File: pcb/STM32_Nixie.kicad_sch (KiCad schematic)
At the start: 0 parts

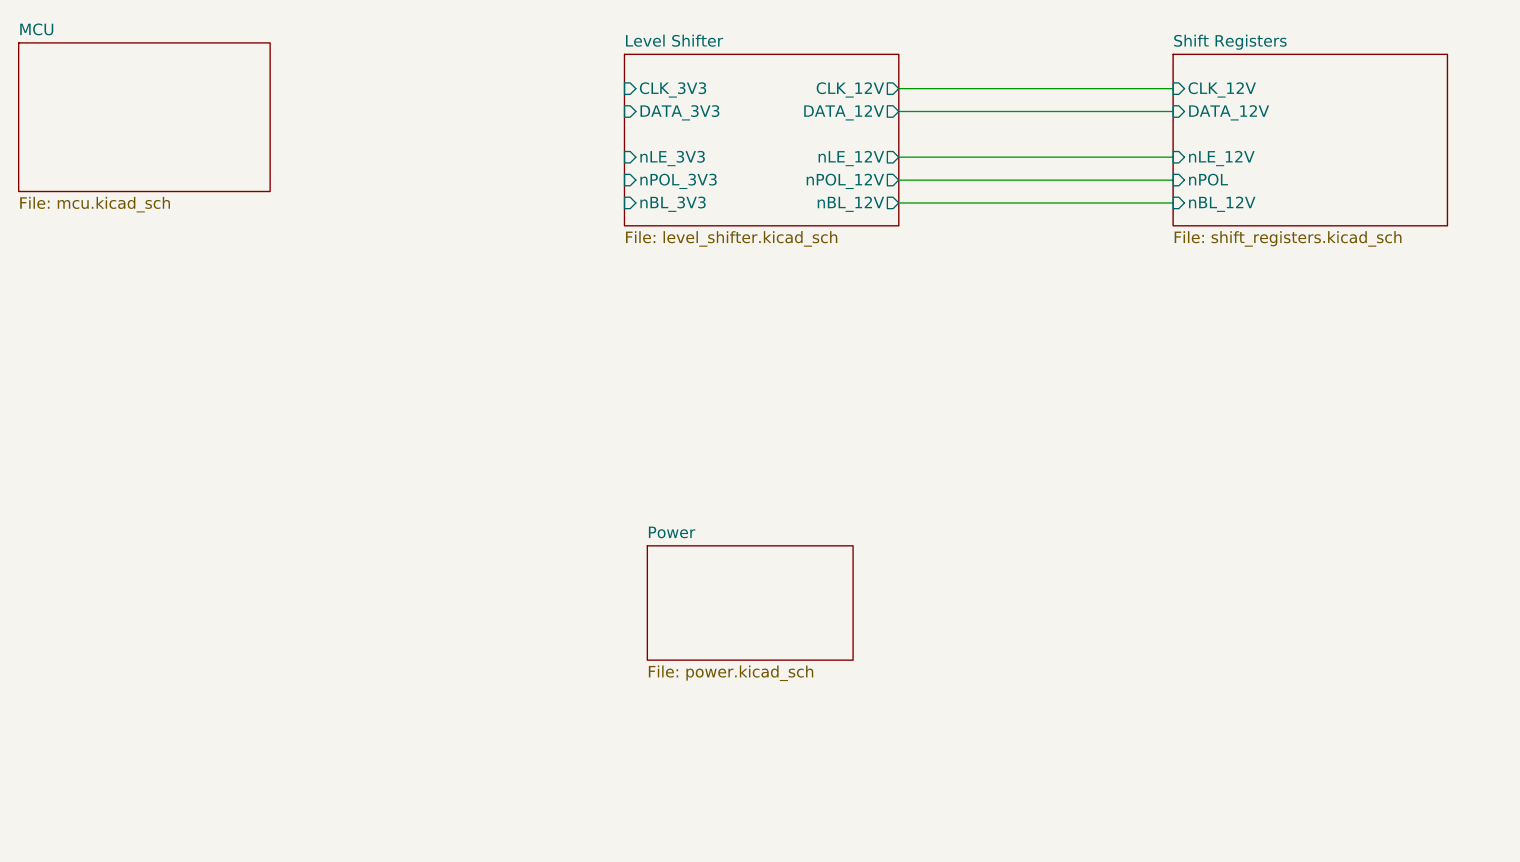
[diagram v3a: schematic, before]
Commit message: Added 8MHz Oscillator and mapped most of the MCU pins"
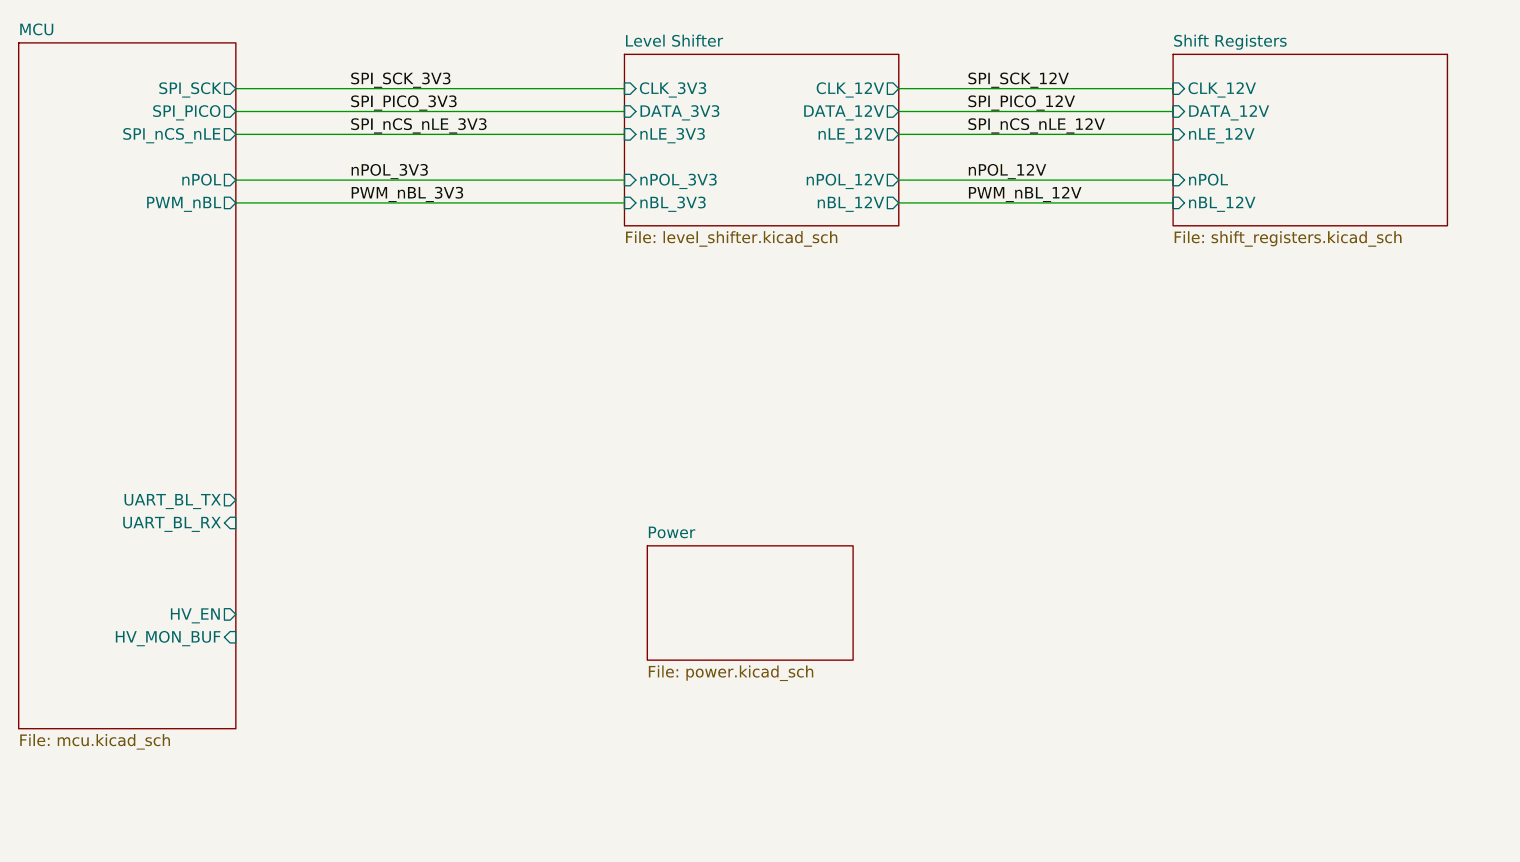
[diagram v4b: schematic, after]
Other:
- sheet MCU ports: added HV_EN, HV_MON_BUF, PWM_nBL, SPI_PICO, SPI_SCK, SPI_nCS_nLE, UART_BL_RX, UART_BL_TX, nPOL; removed none

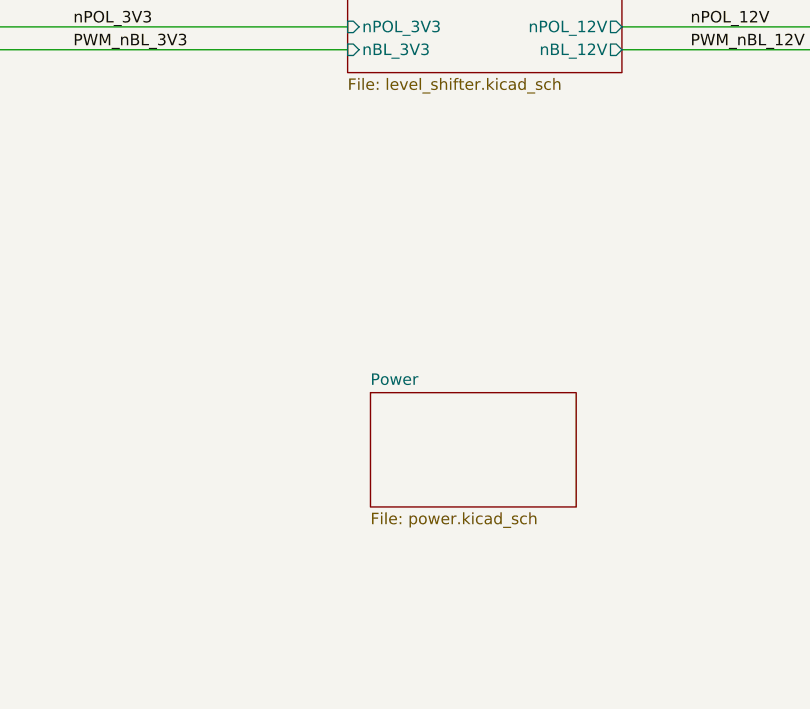
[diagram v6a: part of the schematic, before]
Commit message: Changed Boot0 switch to mom. pb, added rotary encoder, and nRST pb
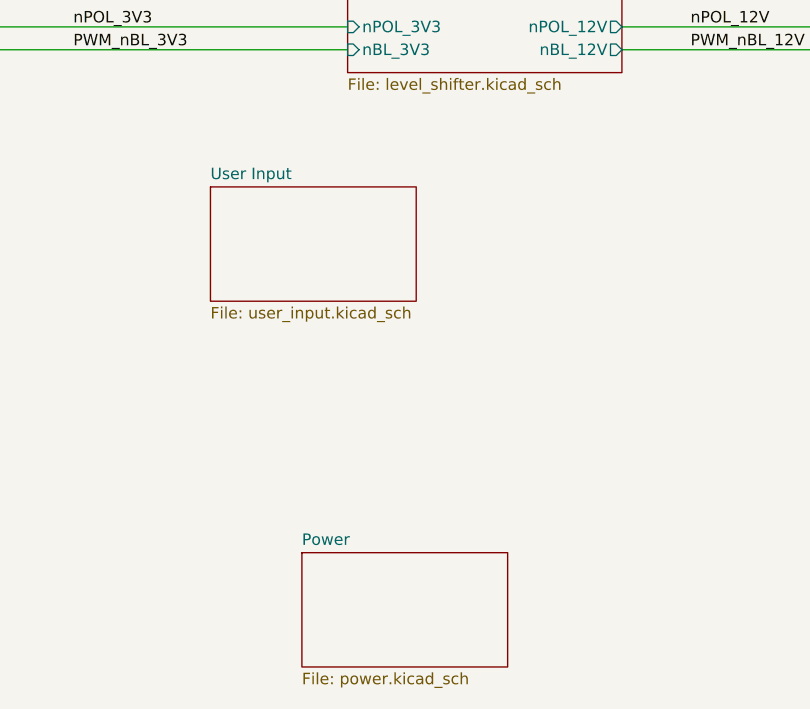
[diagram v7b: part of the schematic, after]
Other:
- added sheet User Input (user_input.kicad_sch)
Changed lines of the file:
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@@
+    )
+  )
+  (sheet (at 119.38 99.06) (size 22.86 12.7) (fields_autoplaced)
+    (stroke (width 0.1524) (type solid) (color 0 0 0 0))
+    (fill (color 0 0 0 0.0000))
+    (property "Sheet name" "User Input" (id 0) (at 119.38 98.3484 0)
+      (effects (font (size 1.27 1.27)) (justify left bottom))
+    )
+    (property "Sheet file" "user_input.kicad_sch" (id 1) (at 119.38 112.3446 0)
+      (effects (font (size 1.27 1.27)) (justify left top))
     )
   )
@@
     )
   )
-  (sheet (at 137.16 121.92) (size 22.86 12.7) (fields_autoplaced)
+  (sheet (at 129.54 139.7) (size 22.86 12.7) (fields_autoplaced)
     (stroke (width 0.1524) (type solid) (color 0 0 0 0))
     (fill (color 0 0 0 0.0000))
-    (property "Sheet name" "Power" (id 0) (at 137.16 121.2084 0)
+    (property "Sheet name" "Power" (id 0) (at 129.54 138.9884 0)
       (effects (font (size 1.27 1.27)) (justify left bottom))
     )
-    (property "Sheet file" "power.kicad_sch" (id 1) (at 137.16 135.2046 0)
+    (property "Sheet file" "power.kicad_sch" (id 1) (at 129.54 152.9846 0)
       (effects (font (size 1.27 1.27)) (justify left top))
     )
@@
     (path "/307c8046-6a25-4c40-9f6b-0df19175f959" (page "10"))
     (path "/b6f49995-0eb9-4525-a397-4f1a1965a188" (page "11"))
+    (path "/7f1e094c-d2d9-45ca-af31-f2b20e969c41" (page "12"))
   )
   (symbol_instances
@@
       (reference "#PWR039") (unit 1) (value "GND") (footprint "")
     )
-    (path "/8ecdbb98-5b2a-4725-a227-62b58d0c66f3/80efdaf2-d5a3-4a81-adba-53a920337fb2"
-      (reference "#PWR?") (unit 1) (value "GND") (footprint "")
+    (path "/8ecdbb98-5b2a-4725-a227-62b58d0c66f3/cf3a7745-9e48-408c-810d-2662e07bc0fd"
+      (reference "#PWR040") (unit 1) (value "GND") (footprint "")
+    )
+    (path "/8ecdbb98-5b2a-4725-a227-62b58d0c66f3/c260bd7e-1970-44f1-8460-f04872940c93"
+      (reference "#PWR041") (unit 1) (value "+3.3V") (footprint "")
+    )
+    (path "/8ecdbb98-5b2a-4725-a227-62b58d0c66f3/e98dab80-82d5-44b0-b230-3d2a8dc0b464"
+      (reference "#PWR042") (unit 1) (value "+3.3V") (footprint "")
     )
     (path "/8ecdbb98-5b2a-4725-a227-62b58d0c66f3/94413c1a-988b-4fe0-9e4f-82a46b39c491"
-      (reference "#PWR?") (unit 1) (value "+3.3V") (footprint "")
-    )
-    (path "/8ecdbb98-5b2a-4725-a227-62b58d0c66f3/c260bd7e-1970-44f1-8460-f04872940c93"
-      (reference "#PWR?") (unit 1) (value "+3.3V") (footprint "")
-    )
-    (path "/8ecdbb98-5b2a-4725-a227-62b58d0c66f3/cf3a7745-9e48-408c-810d-2662e07bc0fd"
-      (reference "#PWR?") (unit 1) (value "GND") (footprint "")
+      (reference "#PWR044") (unit 1) (value "+3.3V") (footprint "")
     )
     (path "/8ecdbb98-5b2a-4725-a227-62b58d0c66f3/e278a8ec-5721-40bf-b2cb-6783be8e79cc"
-      (reference "#PWR?") (unit 1) (value "GND") (footprint "")
-    )
-    (path "/8ecdbb98-5b2a-4725-a227-62b58d0c66f3/e98dab80-82d5-44b0-b230-3d2a8dc0b464"
-      (reference "#PWR?") (unit 1) (value "+3.3V") (footprint "")
+      (reference "#PWR045") (unit 1) (value "GND") (footprint "")
+    )
+    (path "/7f1e094c-d2d9-45ca-af31-f2b20e969c41/e2b85829-8087-4caf-9ed9-28a9ad4f2e8b"
+      (reference "#PWR046") (unit 1) (value "+3.3V") (footprint "")
+    )
+    (path "/7f1e094c-d2d9-45ca-af31-f2b20e969c41/5959c917-a90c-46b2-b99d-437e6ede76e2"
+      (reference "#PWR047") (unit 1) (value "+3.3V") (footprint "")
+    )
+    (path "/7f1e094c-d2d9-45ca-af31-f2b20e969c41/f952946d-ec4b-49ef-8ff1-1d14625955d8"
+      (reference "#PWR048") (unit 1) (value "+3.3V") (footprint "")
+    )
+    (path "/7f1e094c-d2d9-45ca-af31-f2b20e969c41/19018160-5b5b-47ae-84ef-f67b309cee66"
+      (reference "#PWR?") (unit 1) (value "GND") (footprint "")
+    )
+    (path "/7f1e094c-d2d9-45ca-af31-f2b20e969c41/351dfe6b-16a0-4dba-9ac7-f48d92dbd7ed"
+      (reference "#PWR?") (unit 1) (value "GND") (footprint "")
+    )
+    (path "/7f1e094c-d2d9-45ca-af31-f2b20e969c41/47d8c42e-645b-4356-a938-8a84eae8836c"
+      (reference "#PWR?") (unit 1) (value "GND") (footprint "")
+    )
+    (path "/8ecdbb98-5b2a-4725-a227-62b58d0c66f3/47f66aef-bce2-4ea4-8203-d99f7ba5bc8a"
+      (reference "#PWR?") (unit 1) (value "GND") (footprint "")
+    )
+    (path "/7f1e094c-d2d9-45ca-af31-f2b20e969c41/93f56527-ed39-45e7-a1af-7c9fbc290d95"
+      (reference "#PWR?") (unit 1) (value "GND") (footprint "")
+    )
+    (path "/8ecdbb98-5b2a-4725-a227-62b58d0c66f3/97741534-c870-41b3-b484-64d38a10e59f"
+      (reference "#PWR?") (unit 1) (value "GND") (footprint "")
     )
     (path "/8ecdbb98-5b2a-4725-a227-62b58d0c66f3/82d4e7bc-49e8-418b-8c34-f46f3717b905"
@@
       (reference "C19") (unit 1) (value "CAP_CER_4700p_250V_X7R_0805") (footprint "Capacitor_SMD:C_0805_2012Metric")
     )
+    (path "/7f1e094c-d2d9-45ca-af31-f2b20e969c41/4efb7186-35ee-4dab-b3aa-45ce8c158935"
+      (reference "C20") (unit 1) (value "CAP_CER_0u01_50V_X7R_0603") (footprint "Capacitor_SMD:C_0603_1608Metric")
+    )
+    (path "/7f1e094c-d2d9-45ca-af31-f2b20e969c41/8596294f-c74b-4e50-b6cc-c3dc23669cc2"
+      (reference "C21") (unit 1) (value "CAP_CER_0u01_50V_X7R_0603") (footprint "Capacitor_SMD:C_0603_1608Metric")
+    )
+    (path "/7f1e094c-d2d9-45ca-af31-f2b20e969c41/4552bd68-7e86-463c-ba01-3ba48b18d938"
+      (reference "C22") (unit 1) (value "CAP_CER_0u01_50V_X7R_0603") (footprint "Capacitor_SMD:C_0603_1608Metric")
+    )
     (path "/8ecdbb98-5b2a-4725-a227-62b58d0c66f3/f1a32571-49a9-4e57-8b0e-76d78478425a"
       (reference "FB1") (unit 1) (value "FER_1K_600mA_0603") (footprint "Inductor_SMD:L_0603_1608Metric")
@@
     )
     (path "/8ecdbb98-5b2a-4725-a227-62b58d0c66f3/bea2fbe2-f567-481e-90f0-85d9663358e6"
-      (reference "J?") (unit 1) (value "CON_SAMTEC_14P_2R_1m27_P_KEY_FTSH-107-01-L-DV-K-TR") (footprint "arjun_footprints:CON_FTSH-107-01-x-DV-K")
+      (reference "J2") (unit 1) (value "CON_SAMTEC_14P_2R_1m27_P_KEY_FTSH-107-01-L-DV-K-TR") (footprint "arjun_footprints:CON_FTSH-107-01-x-DV-K")
     )
     (path "/8ecdbb98-5b2a-4725-a227-62b58d0c66f3/271153ea-9406-4185-bebd-7bb424efc536"
-      (reference "JP?") (unit 1) (value "SolderJumper_3_Bridged12") (footprint "Jumper:SolderJumper-3_P1.3mm_Bridged12_RoundedPad1.0x1.5mm_NumberLabels")
+      (reference "JP1") (unit 1) (value "SolderJumper_3_Bridged12") (footprint "Jumper:SolderJumper-3_P1.3mm_Bridged12_RoundedPad1.0x1.5mm_NumberLabels")
     )
     (path "/f14ed119-44a4-4dba-a5a7-78813bb44ce1/47fb6452-bb5d-491d-bdc1-b44524035875/592da241-0f55-4f7a-a38f-5ee5a4570347"
@@
     )
     (path "/8ecdbb98-5b2a-4725-a227-62b58d0c66f3/4bdcf741-9b10-451e-b4b3-0d8c758e628e"
-      (reference "R?") (unit 1) (value "RES_10K_1P_1/10W_0603") (footprint "Resistor_SMD:R_0603_1608Metric")
+      (reference "R15") (unit 1) (value "RES_10K_1P_1/10W_0603") (footprint "Resistor_SMD:R_0603_1608Metric")
     )
     (path "/8ecdbb98-5b2a-4725-a227-62b58d0c66f3/4d1cfcde-8dbf-411d-acac-ae2b684de1a4"
-      (reference "R?") (unit 1) (value "RES_10K_1P_1/10W_0603") (footprint "Resistor_SMD:R_0603_1608Metric")
-    )
-    (path "/8ecdbb98-5b2a-4725-a227-62b58d0c66f3/8b537fd6-9959-4c0c-af54-290b92d638d2"
-      (reference "SW?") (unit 1) (value "SW_SPDT_12V_100mA_OS102011MS2QN1") (footprint "arjun_footprints:SW_OS102011MS2QN1")
+      (reference "R16") (unit 1) (value "RES_10K_1P_1/10W_0603") (footprint "Resistor_SMD:R_0603_1608Metric")
+    )
+    (path "/7f1e094c-d2d9-45ca-af31-f2b20e969c41/8aa479a8-4aeb-4d59-a85f-fc41d653df67"
+      (reference "R17") (unit 1) (value "RES_10K_1P_1/10W_0603") (footprint "Resistor_SMD:R_0603_1608Metric")
+    )
+    (path "/7f1e094c-d2d9-45ca-af31-f2b20e969c41/47e1e6e2-cd19-4e54-ab53-5d73e6984888"
+      (reference "R18") (unit 1) (value "RES_10K_1P_1/10W_0603") (footprint "Resistor_SMD:R_0603_1608Metric")
+    )
+    (path "/7f1e094c-d2d9-45ca-af31-f2b20e969c41/5d6e53eb-9333-4cc5-a8b9-529f63aa4c5e"
+      (reference "R19") (unit 1) (value "RES_10K_1P_1/10W_0603") (footprint "Resistor_SMD:R_0603_1608Metric")
+    )
+    (path "/7f1e094c-d2d9-45ca-af31-f2b20e969c41/636a8bd8-74f5-4655-b696-0bd4e9ac7aa8"
+      (reference "R20") (unit 1) (value "RES_10K_1P_1/10W_0603") (footprint "Resistor_SMD:R_0603_1608Metric")
+    )
+    (path "/7f1e094c-d2d9-45ca-af31-f2b20e969c41/22d573b9-e0c9-48fd-a554-d503604a681d"
+      (reference "R21") (unit 1) (value "RES_10K_1P_1/10W_0603") (footprint "Resistor_SMD:R_0603_1608Metric")
+    )
+    (path "/7f1e094c-d2d9-45ca-af31-f2b20e969c41/73d0b36d-8919-47d8-879f-77119241e8cc"
+      (reference "R22") (unit 1) (value "RES_10K_1P_1/10W_0603") (footprint "Resistor_SMD:R_0603_1608Metric")
+    )
+    (path "/8ecdbb98-5b2a-4725-a227-62b58d0c66f3/159a5d4d-bfe6-49ba-aff5-c1b9a6a5332f"
+      (reference "S?") (unit 1) (value "SW_TACT_PTS645SM43SMTR92_LFS") (footprint "arjun_footprints:Switch_Tactile_SMD_6x6mm_PTS645")
+    )
+    (path "/8ecdbb98-5b2a-4725-a227-62b58d0c66f3/664d0758-eeaa-483e-9e05-6ad358541bac"
+      (reference "S?") (unit 1) (value "SW_TACT_PTS645SM43SMTR92_LFS") (footprint "arjun_footprints:Switch_Tactile_SMD_6x6mm_PTS645")
+    )
+    (path "/7f1e094c-d2d9-45ca-af31-f2b20e969c41/3c00b1bc-379e-41be-921f-b00aeb4a7088"
+      (reference "SW2") (unit 1) (value "ENC_SPST_24PPR_PEC12R-4225F-S0024") (footprint "arjun_footprints:ENC_SPST_PEC12R-4x25F-Sxxx")
     )
     (path "/8ecdbb98-5b2a-4725-a227-62b58d0c66f3/461981fc-199c-4e16-9421-bb4b14f2f77f"
@@
     )
     (path "/8ecdbb98-5b2a-4725-a227-62b58d0c66f3/fbc2651c-4065-4451-b357-12462d9334c9"
-      (reference "U3") (unit 1) (value "IC_MCU_STM32F100C4T6B_48LQFP") (footprint "Package_QFP:LQFP-48_7x7mm_P0.5mm")
+      (reference "U3") (unit 1) (value "IC_MCU_STM32F100C4T6B_48LQFP") (footprint "arjun_footprints:LQFP-48_7x7mm_P0.5mm")
     )
     (path "/8ecdbb98-5b2a-4725-a227-62b58d0c66f3/112b520c-8a9f-4f02-838a-ff2913d3cba9"
